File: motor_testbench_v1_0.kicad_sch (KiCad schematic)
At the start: 28 parts, among them IC1 PJA3402_R1_00001, J1 Conn_01x05_Pin, J2 Conn_01x01_Pin, J3 Conn_01x01_Pin, J4 Conn_01x22_Pin, U1 ESP32-S3-DevKitC

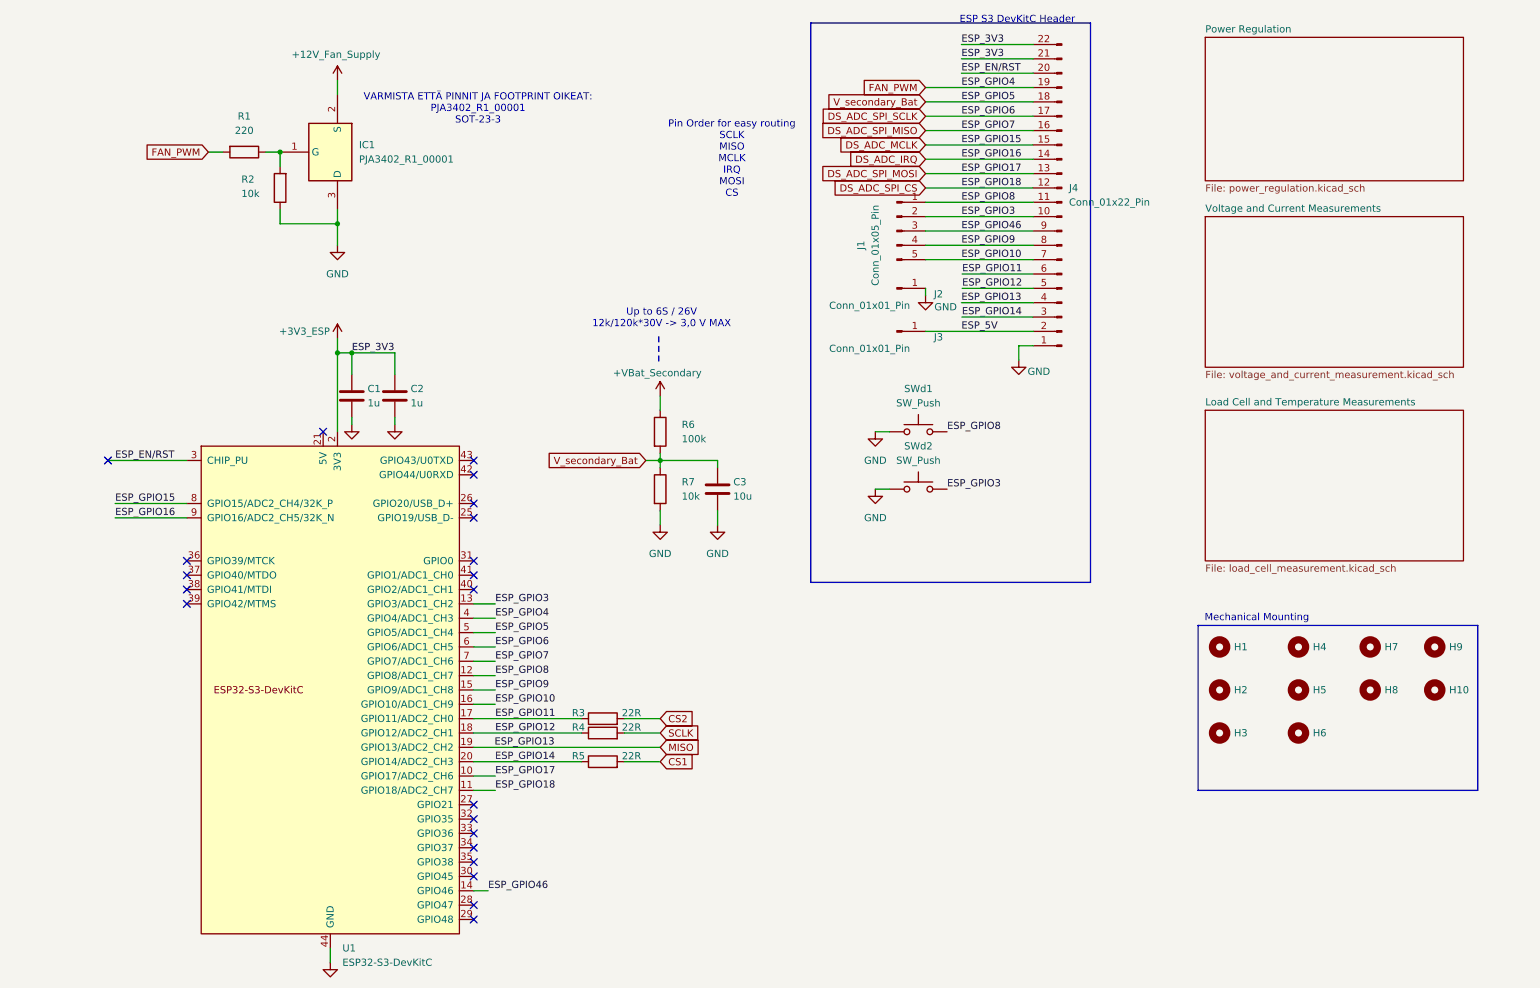
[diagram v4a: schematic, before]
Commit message: Add full ESP32 DevKit Length PCB.
[KiCad Version: 10.0.4]
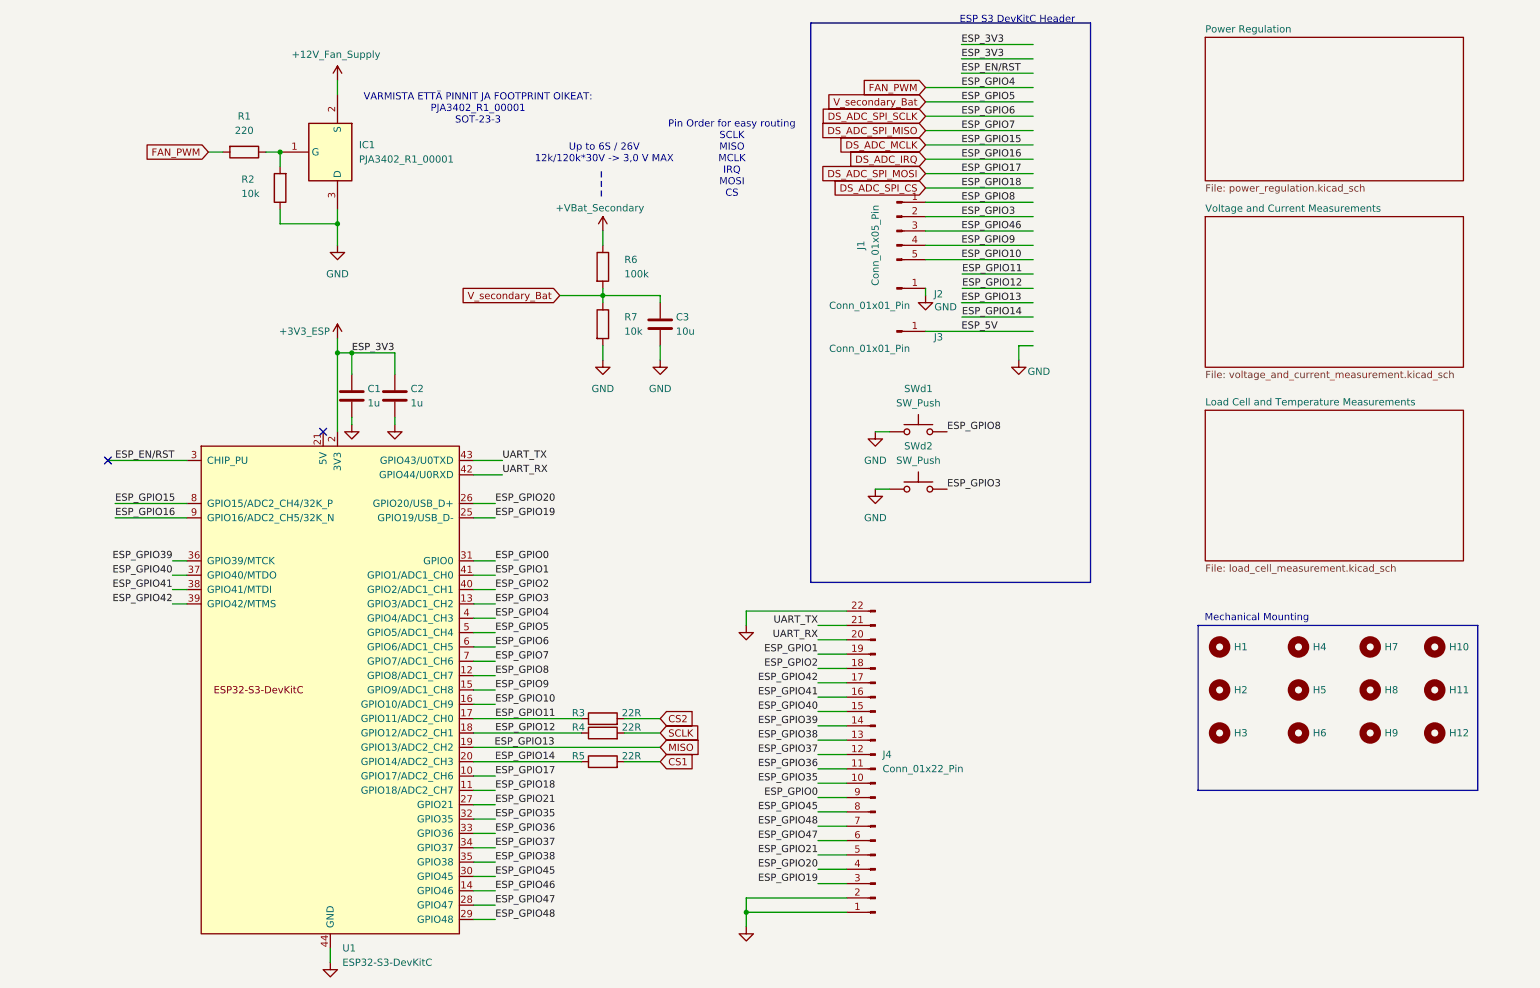
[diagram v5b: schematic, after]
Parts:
- added H12, H9: MountingHole, MountingHole:MountingHole_2.2mm_M2_DIN965, symbol Mechanical:MountingHole
- renumbered H9 to H10, H10 to H11
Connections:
- net +3V3_ESP: no longer J4.21 (Pin_21), J4.22 (Pin_22)
- net DS_ADC_IRQ: no longer J4.14 (Pin_14)
- net DS_ADC_MCLK: no longer J4.15 (Pin_15)
- net DS_ADC_SPI_CS: no longer J4.12 (Pin_12)
- net DS_ADC_SPI_MISO: no longer J4.16 (Pin_16)
- net DS_ADC_SPI_MOSI: no longer J4.13 (Pin_13)
- net DS_ADC_SPI_SCLK: no longer J4.17 (Pin_17)
- net ESP_5V: no longer J4.2 (Pin_2)
- net ESP_EN/RST: no longer J4.20 (Pin_20)
- net ESP_GPIO10: no longer J4.7 (Pin_7)
- net ESP_GPIO11: no longer J4.6 (Pin_6)
- net ESP_GPIO12: no longer J4.5 (Pin_5)
- net ESP_GPIO14: no longer J4.3 (Pin_3)
- net ESP_GPIO3: no longer J4.10 (Pin_10)
- net ESP_GPIO46: no longer J4.9 (Pin_9)
- net ESP_GPIO8: no longer J4.11 (Pin_11)
- net ESP_GPIO9: no longer J4.8 (Pin_8)
- net FAN_PWM: no longer J4.19 (Pin_19)
- net GND: now also J4.2 (Pin_2), J4.22 (Pin_22)
- net MISO: no longer J4.4 (Pin_4)
- net V_secondary_Bat: no longer J4.18 (Pin_18)
- net ESP_GPIO19: now reaches U1.25 (GPIO19/USB_D-)
- net ESP_GPIO19: now also J4.3 (Pin_3)
- net ESP_GPIO20: now reaches U1.26 (GPIO20/USB_D+)
- net ESP_GPIO20: now also J4.4 (Pin_4)
- net ESP_GPIO21: now reaches U1.27 (GPIO21)
- net ESP_GPIO21: now also J4.5 (Pin_5)
- net ESP_GPIO47: now reaches U1.28 (GPIO47)
- net ESP_GPIO47: now also J4.6 (Pin_6)
- net ESP_GPIO48: now reaches U1.29 (GPIO48)
- net ESP_GPIO48: now also J4.7 (Pin_7)
- net ESP_GPIO45: now reaches U1.30 (GPIO45)
- net ESP_GPIO45: now also J4.8 (Pin_8)
- net ESP_GPIO0: now reaches U1.31 (GPIO0)
- net ESP_GPIO0: now also J4.9 (Pin_9)
- net ESP_GPIO35: now reaches U1.32 (GPIO35)
- net ESP_GPIO35: now also J4.10 (Pin_10)
- net ESP_GPIO36: now reaches U1.33 (GPIO36)
- net ESP_GPIO36: now also J4.11 (Pin_11)
- net ESP_GPIO37: now reaches U1.34 (GPIO37)
- net ESP_GPIO37: now also J4.12 (Pin_12)
- net ESP_GPIO38: now reaches U1.35 (GPIO38)
- net ESP_GPIO38: now also J4.13 (Pin_13)
- net ESP_GPIO39: now reaches U1.36 (GPIO39/MTCK)
- net ESP_GPIO39: now also J4.14 (Pin_14)
- net ESP_GPIO40: now reaches U1.37 (GPIO40/MTDO)
- net ESP_GPIO40: now also J4.15 (Pin_15)
- net ESP_GPIO41: now reaches U1.38 (GPIO41/MTDI)
- net ESP_GPIO41: now also J4.16 (Pin_16)
- net ESP_GPIO42: now reaches U1.39 (GPIO42/MTMS)
- net ESP_GPIO42: now also J4.17 (Pin_17)
- net ESP_GPIO2: now reaches U1.40 (GPIO2/ADC1_CH1)
- net ESP_GPIO2: now also J4.18 (Pin_18)
- net ESP_GPIO1: now reaches U1.41 (GPIO1/ADC1_CH0)
- net ESP_GPIO1: now also J4.19 (Pin_19)
- net UART_RX: now reaches U1.42 (GPIO44/U0RXD)
- net UART_RX: now also J4.20 (Pin_20)
- net UART_TX: now reaches U1.43 (GPIO43/U0TXD)
- net UART_TX: now also J4.21 (Pin_21)
- no-connect marks 21 -> 2
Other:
- moved on the sheet: C3, J4, R6, R7
